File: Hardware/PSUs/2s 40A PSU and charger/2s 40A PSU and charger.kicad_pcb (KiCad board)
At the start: 4 copper layers, 45 x 20 mm, 112 parts, among them J1 Keystone 3579, J10 G-Switch-GT-USB-7025, J11 1.27mm 4 pin socket, J12 USB, J2 JST XH-S Balance Plug, J3 Keystone 3579, J4 Keystone 3569, J5 Keystone 3569, J6 Keystone 3579, J7 Keystone 3579, J8 Keystone 3569, J9 Keystone 3569, Q1 PJA3430, or HL 2320A, Q2 PJA3430, or HL 2320A, Q3 Vishay sir404dp, or SiR500DP, Q4 PJA3430, or HL 2320A, Q5 PJA3430, or HL 2320A, Q6 Vishay sir404dp, or SiR500DP, U1 BQ76905RGRR, U2 AP63203WU, U3 BQ24780SRUYR, U5 THVD1420DRLR, U6 CH32X035G8U6, U7 TPS7A2633DRV

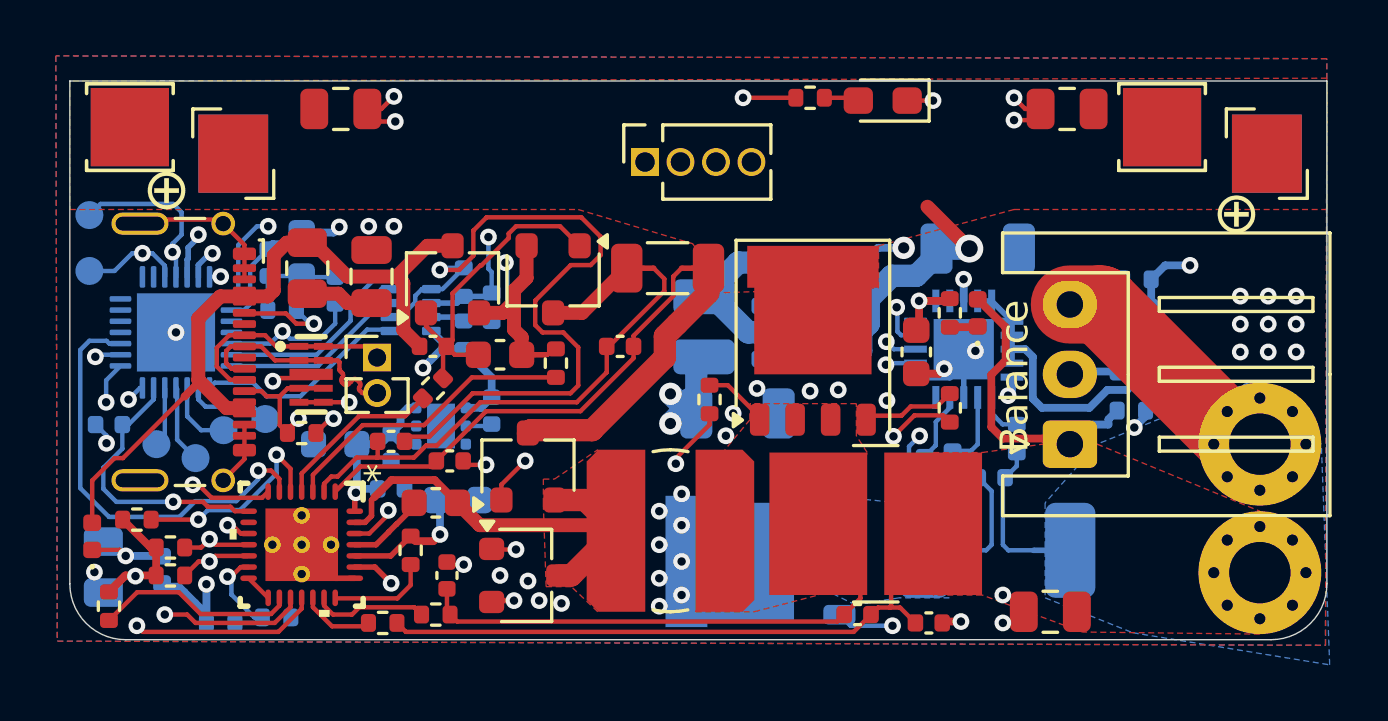
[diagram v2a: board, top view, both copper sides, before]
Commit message: Fixed issue with USB-C pad spacing on 2oz copper
The minimum spacing between tracks on 2oz copper is 0.16mm, and I had explicitly ignored the USB-C connector pin spacing 0.12mm in a custom DRC rule, which turned out to be a problem. I removed that rule and modified the USB-C connector pads to be slightly narrower to give more gap.
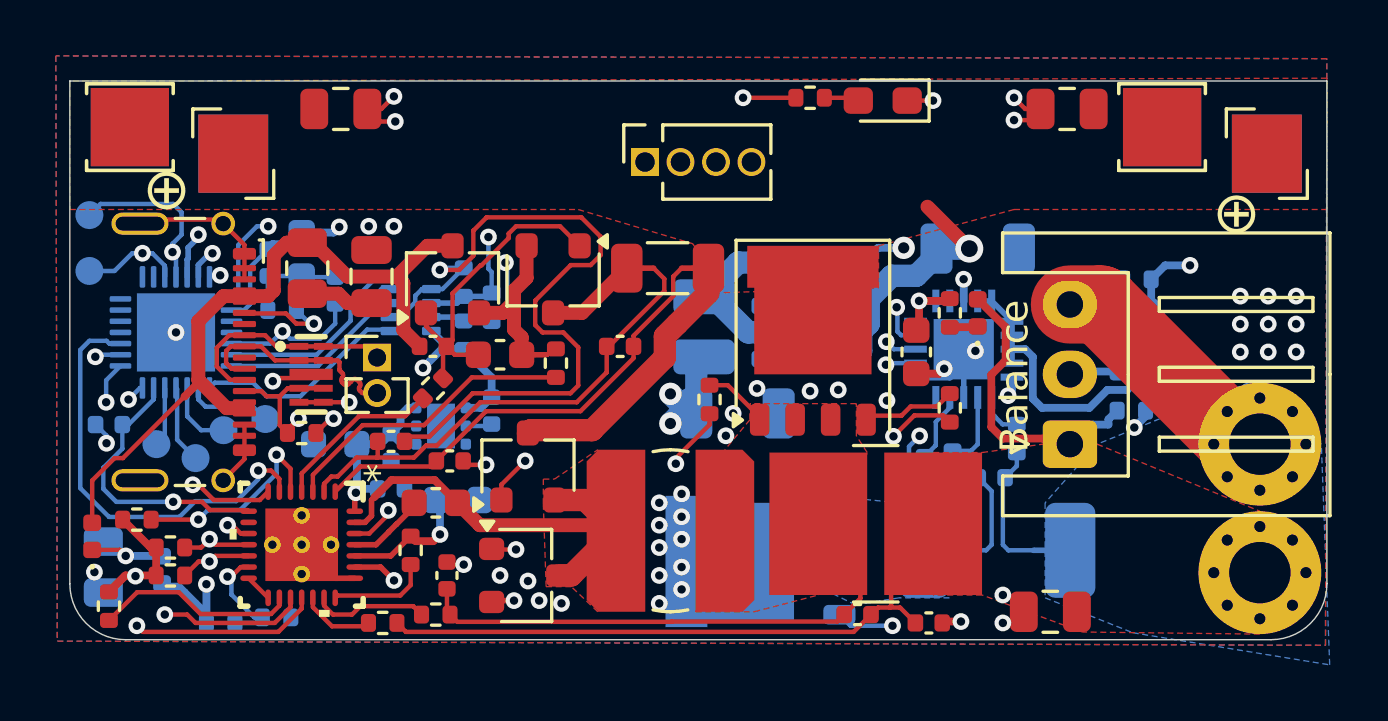
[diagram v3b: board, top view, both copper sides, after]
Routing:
- net GND: vias 45 -> 47
